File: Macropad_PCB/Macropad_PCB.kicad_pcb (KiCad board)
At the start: 2 copper layers, 3 parts, among them SW1 SW_Push, SW2 RotaryEncoder, U1 MOUDLE-SEEEDUINO-XIAO

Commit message: Inizio PCB
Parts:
- removed SW1: SW_Push, Button_Switch_Keyboard:SW_Cherry_MX_1.00u_PCB
- added J1: OLED_128x32, ScottoKeebs_Components:OLED_128x32, F.Cu at (51.6, 29.2)
- added S1: ~, ScottoKeebs_MX:MX_PCB_1.00u, F.Cu at (47.0, 52.5)
- added S10: ~, ScottoKeebs_MX:MX_PCB_1.00u, F.Cu at (66.0, 90.6)
- added S11: ~, ScottoKeebs_MX:MX_PCB_1.00u, F.Cu at (85.1, 90.6)
- added S12: ~, ScottoKeebs_MX:MX_PCB_1.00u, F.Cu at (104.1, 90.6)
- added S2: ~, ScottoKeebs_MX:MX_PCB_1.00u, F.Cu at (66.0, 52.5)
- added S3: ~, ScottoKeebs_MX:MX_PCB_1.00u, F.Cu at (85.1, 52.5)
- added S4: ~, ScottoKeebs_MX:MX_PCB_1.00u, F.Cu at (104.1, 52.5)
- added S5: ~, ScottoKeebs_MX:MX_PCB_1.00u, F.Cu at (47.0, 71.5)
- added S6: ~, ScottoKeebs_MX:MX_PCB_1.00u, F.Cu at (66.0, 71.5)
- added S7: ~, ScottoKeebs_MX:MX_PCB_1.00u, F.Cu at (85.1, 71.5)
- added S8: ~, ScottoKeebs_MX:MX_PCB_1.00u, F.Cu at (104.1, 71.5)
- added S9: ~, ScottoKeebs_MX:MX_PCB_1.00u, F.Cu at (47.0, 90.6)
- moved SW0 21.8 mm to (99.7, 22.0)
- moved U1 10.8 mm to (73.5, 25.0)
- renumbered SW2 to SW0
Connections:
- SW0 pad A: unconnected-(SW2-PadA) -> RodeaA
- SW0 pad B: unconnected-(SW2-PadB) -> RodeaB
- SW0 pad C: unconnected-(SW2-PadC) -> GND
- U1 pad 1: unconnected-(U1-PA02_A0_D0-Pad1) -> Col0
- U1 pad 10: unconnected-(U1-PA5_A9_D9_MISO-Pad10) -> RodeaB
- U1 pad 11: unconnected-(U1-PA6_A10_D10_MOSI-Pad11) -> RodeaA
- U1 pad 12: unconnected-(U1-3V3-Pad12) -> +3.3V
- U1 pad 13: unconnected-(U1-GND-Pad13) -> GND
- U1 pad 14: unconnected-(U1-5V-Pad14) -> +5V
- U1 pad 2: unconnected-(U1-PA4_A1_D1-Pad2) -> Col1
- U1 pad 3: unconnected-(U1-PA10_A2_D2-Pad3) -> Col2
- U1 pad 4: unconnected-(U1-PA11_A3_D3-Pad4) -> Col3
- U1 pad 5: unconnected-(U1-PA8_A4_D4_SDA-Pad5) -> SDA
- U1 pad 6: unconnected-(U1-PA9_A5_D5_SCL-Pad6) -> SCL
- U1 pad 7: unconnected-(U1-PB08_A6_D6_TX-Pad7) -> Row2
- U1 pad 8: unconnected-(U1-PB09_A7_D7_RX-Pad8) -> Row1
- U1 pad 9: unconnected-(U1-PA7_A8_D8_SCK-Pad9) -> Row0
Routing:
- net GND: track 0.00 -> 63.9 mm
- net +3.3V: track 0.00 -> 37.8 mm
- net SCL: track 0.00 -> 26.0 mm
- net RodeaA: track 0.00 -> 20.6 mm
- net RodeaB: track 0.00 -> 18.9 mm
- net SDA: track 0.00 -> 16.0 mm

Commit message: PCB. Ancora alcuni errori
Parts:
- added D1: ~, ScottoKeebs_Components:Diode_DO-35, F.Cu at (39.0, 52.8)
- added D10: ~, ScottoKeebs_Components:Diode_DO-35, F.Cu at (58.1, 90.9)
- added D11: ~, ScottoKeebs_Components:Diode_DO-35, F.Cu at (77.1, 90.9)
- added D12: ~, ScottoKeebs_Components:Diode_DO-35, F.Cu at (96.2, 90.9)
- added D2: ~, ScottoKeebs_Components:Diode_DO-35, F.Cu at (58.1, 52.8)
- added D3: ~, ScottoKeebs_Components:Diode_DO-35, F.Cu at (77.1, 52.8)
- added D4: ~, ScottoKeebs_Components:Diode_DO-35, F.Cu at (96.2, 52.8)
- added D5: ~, ScottoKeebs_Components:Diode_DO-35, F.Cu at (39.0, 71.8)
- added D6: ~, ScottoKeebs_Components:Diode_DO-35, F.Cu at (58.1, 71.8)
- added D7: ~, ScottoKeebs_Components:Diode_DO-35, F.Cu at (77.1, 71.8)
- added D8: ~, ScottoKeebs_Components:Diode_DO-35, F.Cu at (96.2, 71.8)
- added D9: ~, ScottoKeebs_Components:Diode_DO-35, F.Cu at (39.0, 90.9)
- moved S10 17.8 mm to (48.5, 87.1)
- moved S11 17.8 mm to (67.6, 87.1)
- moved S12 17.8 mm to (86.6, 87.1)
- moved S2 17.8 mm to (48.5, 49.0)
- moved S3 17.8 mm to (67.6, 49.0)
- moved S4 17.8 mm to (86.6, 49.0)
- moved S6 17.8 mm to (48.5, 68.0)
- moved S7 17.8 mm to (67.6, 68.0)
- moved S8 17.8 mm to (86.6, 68.0)
- moved S1 17.8 mm to (29.5, 49.0)
- moved S5 17.8 mm to (29.5, 68.0)
- moved S9 17.8 mm to (29.5, 87.1)
- moved SW0 11.0 mm to (88.7, 22.0)
- moved U1 3.50 mm to (70.0, 25.0)
- moved J1 3.40 mm to (55.0, 29.2)
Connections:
- U1 pad 1: Col0 -> Col3
- U1 pad 2: Col1 -> Col2
- U1 pad 3: Col2 -> Col1
- U1 pad 4: Col3 -> Col0
- U1 pad 8: Row1 -> Row0
- U1 pad 9: Row0 -> Row1
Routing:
- net Row2: track 0.00 -> 176.8 mm
- net Row1: track 0.00 -> 123.1 mm
- net Col0: track 0.00 -> 104.5 mm
- net Row0: track 0.00 -> 98.4 mm
- net Col1: track 0.00 -> 90.1 mm
- net Col3: track 0.00 -> 78.0 mm
- net Col2: track 0.00 -> 74.3 mm
- net GND: track 63.9 -> 49.0 mm
- net RodeaA: track 20.6 -> 12.4 mm
- net SCL: track 26.0 -> 18.2 mm
- net RodeaB: track 18.9 -> 11.3 mm
- net Net-(D6-A): track 0.00 -> 7.55 mm
- net Net-(D7-A): track 0.00 -> 7.55 mm
- net Net-(D8-A): track 0.00 -> 7.51 mm
- net Net-(D5-A): track 0.00 -> 7.51 mm
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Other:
- board outline added: 91 x 85 mm

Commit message: PCB
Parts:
- moved J1 3.06 mm to (56.1, 32.1)
- moved SW0 2.81 mm to (86.7, 23.9)
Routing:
- net RodeaA: track 12.4 -> 9.57 mm
- net +3.3V: track 31.8 -> 33.7 mm
- net RodeaB: track 11.3 -> 9.72 mm
- net GND: track 49.0 -> 50.4 mm
- net Row2: track 176.8 -> 176.0 mm
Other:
- board size 91 x 85 mm -> 91 x 85.5 mm

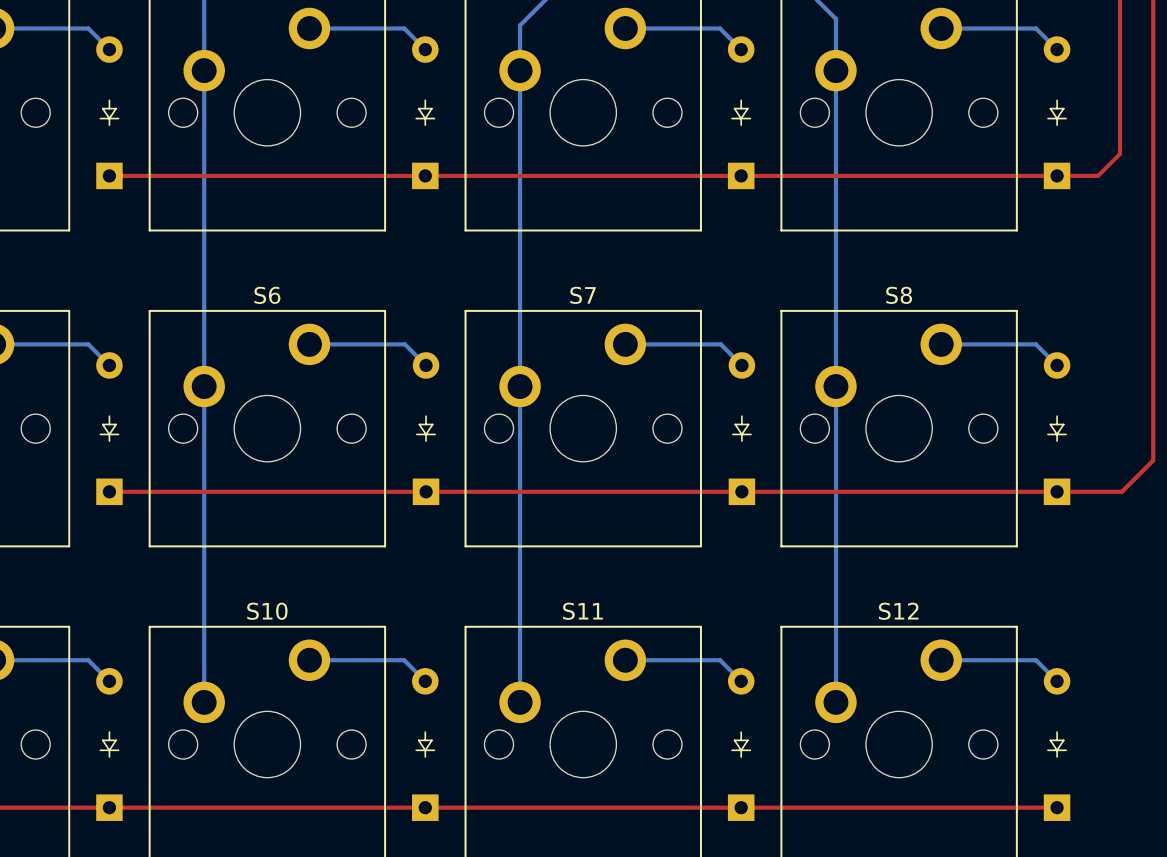
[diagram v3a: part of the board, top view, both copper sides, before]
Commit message: Diodes on PCB back
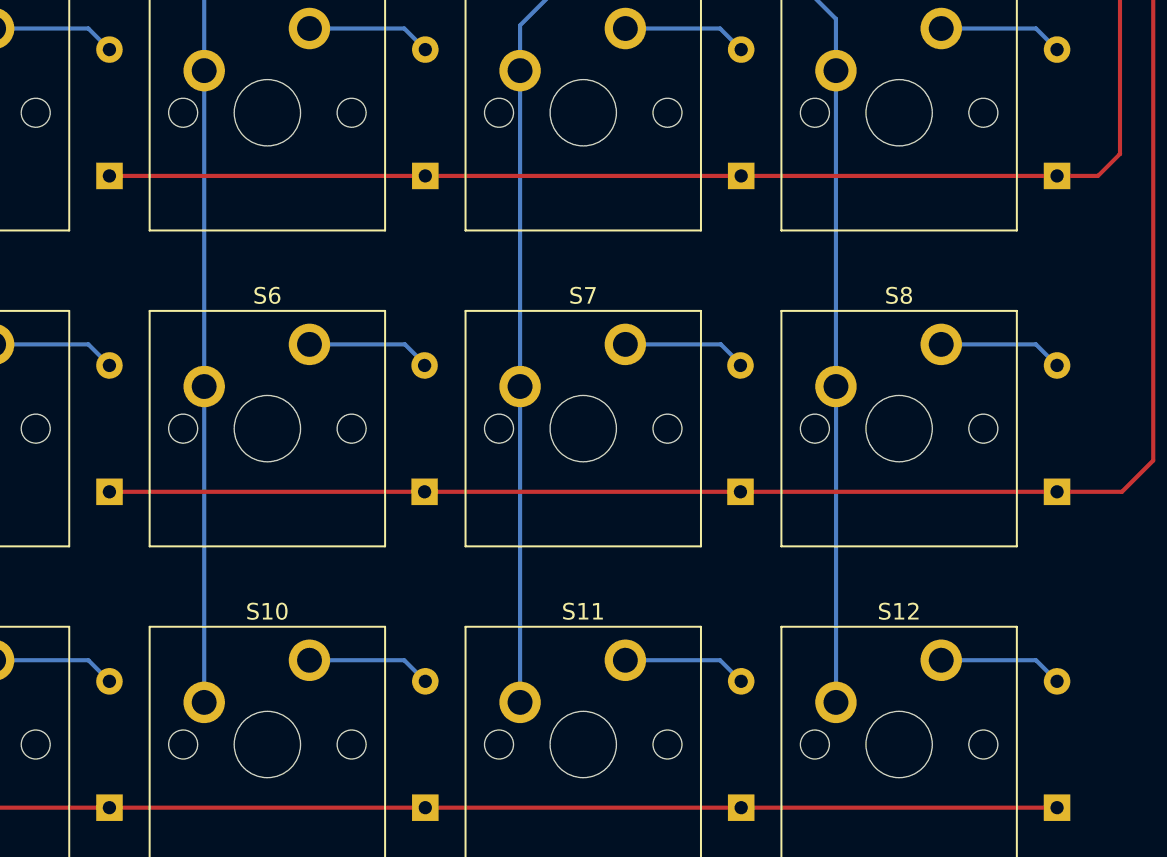
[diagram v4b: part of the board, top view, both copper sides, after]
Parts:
- D1, D10, D11, D12, D2, D3, D4, D5, D6, D7, D8, D9: moved to B.Cu
- moved D1 57.1 mm to (96.2, 52.8)
- moved D12 57.1 mm to (39.0, 90.9)
- moved D4 57.1 mm to (39.0, 52.8)
- moved D5 57.1 mm to (96.2, 71.8)
- moved D8 57.1 mm to (39.0, 71.8)
- moved D9 57.1 mm to (96.2, 90.9)
- moved D7 19.1 mm to (58.0, 71.8)
- moved D10 19.1 mm to (77.1, 90.9)
- moved D11 19.1 mm to (58.1, 90.9)
- moved D2 19.1 mm to (77.1, 52.8)
- moved D3 19.1 mm to (58.1, 52.8)
- moved D6 19.0 mm to (77.1, 71.8)

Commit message: Correzione errori CC
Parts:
- moved D1 57.1 mm to (39.0, 52.8)
- moved D12 57.1 mm to (96.2, 90.9)
- moved D4 57.1 mm to (96.2, 52.8)
- moved D5 57.1 mm to (39.0, 71.8)
- moved D8 57.1 mm to (96.2, 71.8)
- moved D9 57.1 mm to (39.0, 90.9)
- moved D7 19.1 mm to (77.1, 71.8)
- moved D10 19.1 mm to (58.1, 90.9)
- moved D11 19.1 mm to (77.1, 90.9)
- moved D2 19.1 mm to (58.1, 52.8)
- moved D3 19.1 mm to (77.1, 52.8)
- moved D6 19.0 mm to (58.1, 71.8)
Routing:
- added copper zone on B.Cu, net GND
- added copper zone on F.Cu, net GND
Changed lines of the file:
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@@
 	(footprint "ScottoKeebs_Components:Diode_DO-35"
 		(layer "B.Cu")
-		(at 77.105 90.885 90)
+		(at 58.055 90.885 90)
 		(descr "Diode, DO-35_SOD27 series, Axial, Horizontal, pin pitch=7.62mm, , length*diameter=4*2mm^2, , http://www.diodes.com/_files/packages/DO-35.pdf")
 		(tags "Diode DO-35_SOD27 series Axial Horizontal pin pitch 7.62mm  length 4mm diameter 2mm")
@@
 	(footprint "ScottoKeebs_Components:Diode_DO-35"
 		(layer "B.Cu")
-		(at 39.005 52.785 90)
+		(at 96.155 52.785 90)
 		(descr "Diode, DO-35_SOD27 series, Axial, Horizontal, pin pitch=7.62mm, , length*diameter=4*2mm^2, , http://www.diodes.com/_files/packages/DO-35.pdf")
 		(tags "Diode DO-35_SOD27 series Axial Horizontal pin pitch 7.62mm  length 4mm diameter 2mm")
@@
 	(footprint "ScottoKeebs_Components:Diode_DO-35"
 		(layer "B.Cu")
-		(at 77.06125 71.835 90)
+		(at 58.09875 71.835 90)
 		(descr "Diode, DO-35_SOD27 series, Axial, Horizontal, pin pitch=7.62mm, , length*diameter=4*2mm^2, , http://www.diodes.com/_files/packages/DO-35.pdf")
 		(tags "Diode DO-35_SOD27 series Axial Horizontal pin pitch 7.62mm  length 4mm diameter 2mm")
@@
 	(footprint "ScottoKeebs_Components:Diode_DO-35"
 		(layer "B.Cu")
-		(at 58.055 90.885 90)
+		(at 77.105 90.885 90)
 		(descr "Diode, DO-35_SOD27 series, Axial, Horizontal, pin pitch=7.62mm, , length*diameter=4*2mm^2, , http://www.diodes.com/_files/packages/DO-35.pdf")
 		(tags "Diode DO-35_SOD27 series Axial Horizontal pin pitch 7.62mm  length 4mm diameter 2mm")
@@
 	(footprint "ScottoKeebs_Components:Diode_DO-35"
 		(layer "B.Cu")
-		(at 39.005 90.885 90)
+		(at 96.155 90.885 90)
 		(descr "Diode, DO-35_SOD27 series, Axial, Horizontal, pin pitch=7.62mm, , length*diameter=4*2mm^2, , http://www.diodes.com/_files/packages/DO-35.pdf")
 		(tags "Diode DO-35_SOD27 series Axial Horizontal pin pitch 7.62mm  length 4mm diameter 2mm")
@@
 	(footprint "ScottoKeebs_Components:Diode_DO-35"
 		(layer "B.Cu")
-		(at 96.155 52.785 90)
+		(at 39.005 52.785 90)
 		(descr "Diode, DO-35_SOD27 series, Axial, Horizontal, pin pitch=7.62mm, , length*diameter=4*2mm^2, , http://www.diodes.com/_files/packages/DO-35.pdf")
 		(tags "Diode DO-35_SOD27 series Axial Horizontal pin pitch 7.62mm  length 4mm diameter 2mm")
@@
 	(footprint "ScottoKeebs_Components:Diode_DO-35"
 		(layer "B.Cu")
-		(at 39.005 71.835 90)
+		(at 96.155 71.835 90)
 		(descr "Diode, DO-35_SOD27 series, Axial, Horizontal, pin pitch=7.62mm, , length*diameter=4*2mm^2, , http://www.diodes.com/_files/packages/DO-35.pdf")
 		(tags "Diode DO-35_SOD27 series Axial Horizontal pin pitch 7.62mm  length 4mm diameter 2mm")
@@
 	(footprint "ScottoKeebs_Components:Diode_DO-35"
 		(layer "B.Cu")
-		(at 77.105 52.785 90)
+		(at 58.055 52.785 90)
 		(descr "Diode, DO-35_SOD27 series, Axial, Horizontal, pin pitch=7.62mm, , length*diameter=4*2mm^2, , http://www.diodes.com/_files/packages/DO-35.pdf")
 		(tags "Diode DO-35_SOD27 series Axial Horizontal pin pitch 7.62mm  length 4mm diameter 2mm")
@@
 	(footprint "ScottoKeebs_Components:Diode_DO-35"
 		(layer "B.Cu")
-		(at 58.01125 71.835 90)
+		(at 77.14875 71.835 90)
 		(descr "Diode, DO-35_SOD27 series, Axial, Horizontal, pin pitch=7.62mm, , length*diameter=4*2mm^2, , http://www.diodes.com/_files/packages/DO-35.pdf")
 		(tags "Diode DO-35_SOD27 series Axial Horizontal pin pitch 7.62mm  length 4mm diameter 2mm")
@@
 	(footprint "ScottoKeebs_Components:Diode_DO-35"
 		(layer "B.Cu")
-		(at 96.155 71.835 90)
+		(at 39.005 71.835 90)
 		(descr "Diode, DO-35_SOD27 series, Axial, Horizontal, pin pitch=7.62mm, , length*diameter=4*2mm^2, , http://www.diodes.com/_files/packages/DO-35.pdf")
 		(tags "Diode DO-35_SOD27 series Axial Horizontal pin pitch 7.62mm  length 4mm diameter 2mm")
@@
 	(footprint "ScottoKeebs_Components:Diode_DO-35"
 		(layer "B.Cu")
-		(at 58.055 52.785 90)
+		(at 77.105 52.785 90)
 		(descr "Diode, DO-35_SOD27 series, Axial, Horizontal, pin pitch=7.62mm, , length*diameter=4*2mm^2, , http://www.diodes.com/_files/packages/DO-35.pdf")
 		(tags "Diode DO-35_SOD27 series Axial Horizontal pin pitch 7.62mm  length 4mm diameter 2mm")
@@
 	(footprint "ScottoKeebs_Components:Diode_DO-35"
 		(layer "B.Cu")
-		(at 96.155 90.885 90)
+		(at 39.005 90.885 90)
 		(descr "Diode, DO-35_SOD27 series, Axial, Horizontal, pin pitch=7.62mm, , length*diameter=4*2mm^2, , http://www.diodes.com/_files/packages/DO-35.pdf")
 		(tags "Diode DO-35_SOD27 series Axial Horizontal pin pitch 7.62mm  length 4mm diameter 2mm")
@@
 		(end 39.005 45.165)
 		(width 0.25)
-		(layer "B.Cu")
+		(layer "F.Cu")
 		(net 1)
 	)
@@
 		(end 37.735 43.895)
 		(width 0.25)
-		(layer "B.Cu")
+		(layer "F.Cu")
 		(net 1)
 	)
@@
 		(end 58.055 45.165)
 		(width 0.25)
-		(layer "B.Cu")
+		(layer "F.Cu")
 		(net 3)
 	)
@@
 		(end 56.785 43.895)
 		(width 0.25)
-		(layer "B.Cu")
+		(layer "F.Cu")
 		(net 3)
 	)
@@
 		(end 77.105 45.165)
 		(width 0.25)
-		(layer "B.Cu")
+		(layer "F.Cu")
 		(net 6)
 	)
@@
 		(end 75.835 43.895)
 		(width 0.25)
-		(layer "B.Cu")
+		(layer "F.Cu")
 		(net 6)
 	)
@@
 		(end 94.885 43.895)
 		(width 0.25)
-		(layer "B.Cu")
+		(layer "F.Cu")
 		(net 7)
 	)
@@
 		(end 96.155 45.165)
 		(width 0.25)
-		(layer "B.Cu")
+		(layer "F.Cu")
 		(net 7)
 	)
@@
 		(end 37.735 62.945)
 		(width 0.25)
-		(layer "B.Cu")
+		(layer "F.Cu")
 		(net 9)
 	)
@@
 		(end 39.005 64.215)
 		(width 0.25)
-		(layer "B.Cu")
+		(layer "F.Cu")
 		(net 9)
 	)
@@
 		(end 56.82875 62.945)
 		(width 0.25)
-		(layer "B.Cu")
+		(layer "F.Cu")
 		(net 10)
 	)
@@
 		(end 58.09875 64.215)
 		(width 0.25)
-		(layer "B.Cu")
+		(layer "F.Cu")
 		(net 10)
 	)
@@
 		(end 75.87875 62.945)
 		(width 0.25)
-		(layer "B.Cu")
+		(layer "F.Cu")
 		(net 11)
 	)
@@
 		(end 77.14875 64.215)
 		(width 0.25)
-		(layer "B.Cu")
+		(layer "F.Cu")
 		(net 11)
 	)
@@
 		(end 96.155 64.215)
 		(width 0.25)
-		(layer "B.Cu")
+		(layer "F.Cu")
 		(net 12)
 	)
@@
 		(end 94.885 62.945)
 		(width 0.25)
-		(layer "B.Cu")
+		(layer "F.Cu")
 		(net 12)
 	)
@@
 		(end 39.005 83.265)
 		(width 0.25)
-		(layer "B.Cu")
+		(layer "F.Cu")
 		(net 13)
 	)
@@
 		(end 37.735 81.995)
 		(width 0.25)
-		(layer "B.Cu")
+		(layer "F.Cu")
 		(net 13)
 	)
@@
 		(end 58.055 83.265)
 		(width 0.25)
-		(layer "B.Cu")
+		(layer "F.Cu")
 		(net 14)
 	)
@@
 		(end 56.785 81.995)
 		(width 0.25)
-		(layer "B.Cu")
+		(layer "F.Cu")
 		(net 14)
 	)
@@
 		(end 77.105 83.265)
 		(width 0.25)
-		(layer "B.Cu")
+		(layer "F.Cu")
 		(net 15)
 	)
@@
 		(end 75.835 81.995)
 		(width 0.25)
-		(layer "B.Cu")
+		(layer "F.Cu")
 		(net 15)
 	)
@@
 		(end 96.155 83.265)
 		(width 0.25)
-		(layer "B.Cu")
+		(layer "F.Cu")
 		(net 20)
 	)
@@
 		(end 94.885 81.995)
 		(width 0.25)
-		(layer "B.Cu")
+		(layer "F.Cu")
 		(net 20)
 	)
@@
 		(net 26)
 	)
+	(zone
+		(net 18)
+		(net_name "GND")
+		(layers "F.Cu" "B.Cu")
+		(hatch edge 0.5)
+		(connect_pads
+			(clearance 0.5)
+		)
+		(min_thickness 0.25)
+		(filled_areas_thickness no)
+		(fill yes
+			(thermal_gap 0.5)
+			(thermal_bridge_width 0.5)
+		)
+		(polygon
+			(pts
+				(xy 9.455 7.95) (xy 115.455 6.95) (xy 114.955 99.95) (xy 3.455 106.45)
+			)
+		)
+	)
 	(embedded_fonts no)
